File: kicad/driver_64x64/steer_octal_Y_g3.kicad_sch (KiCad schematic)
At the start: 66 parts

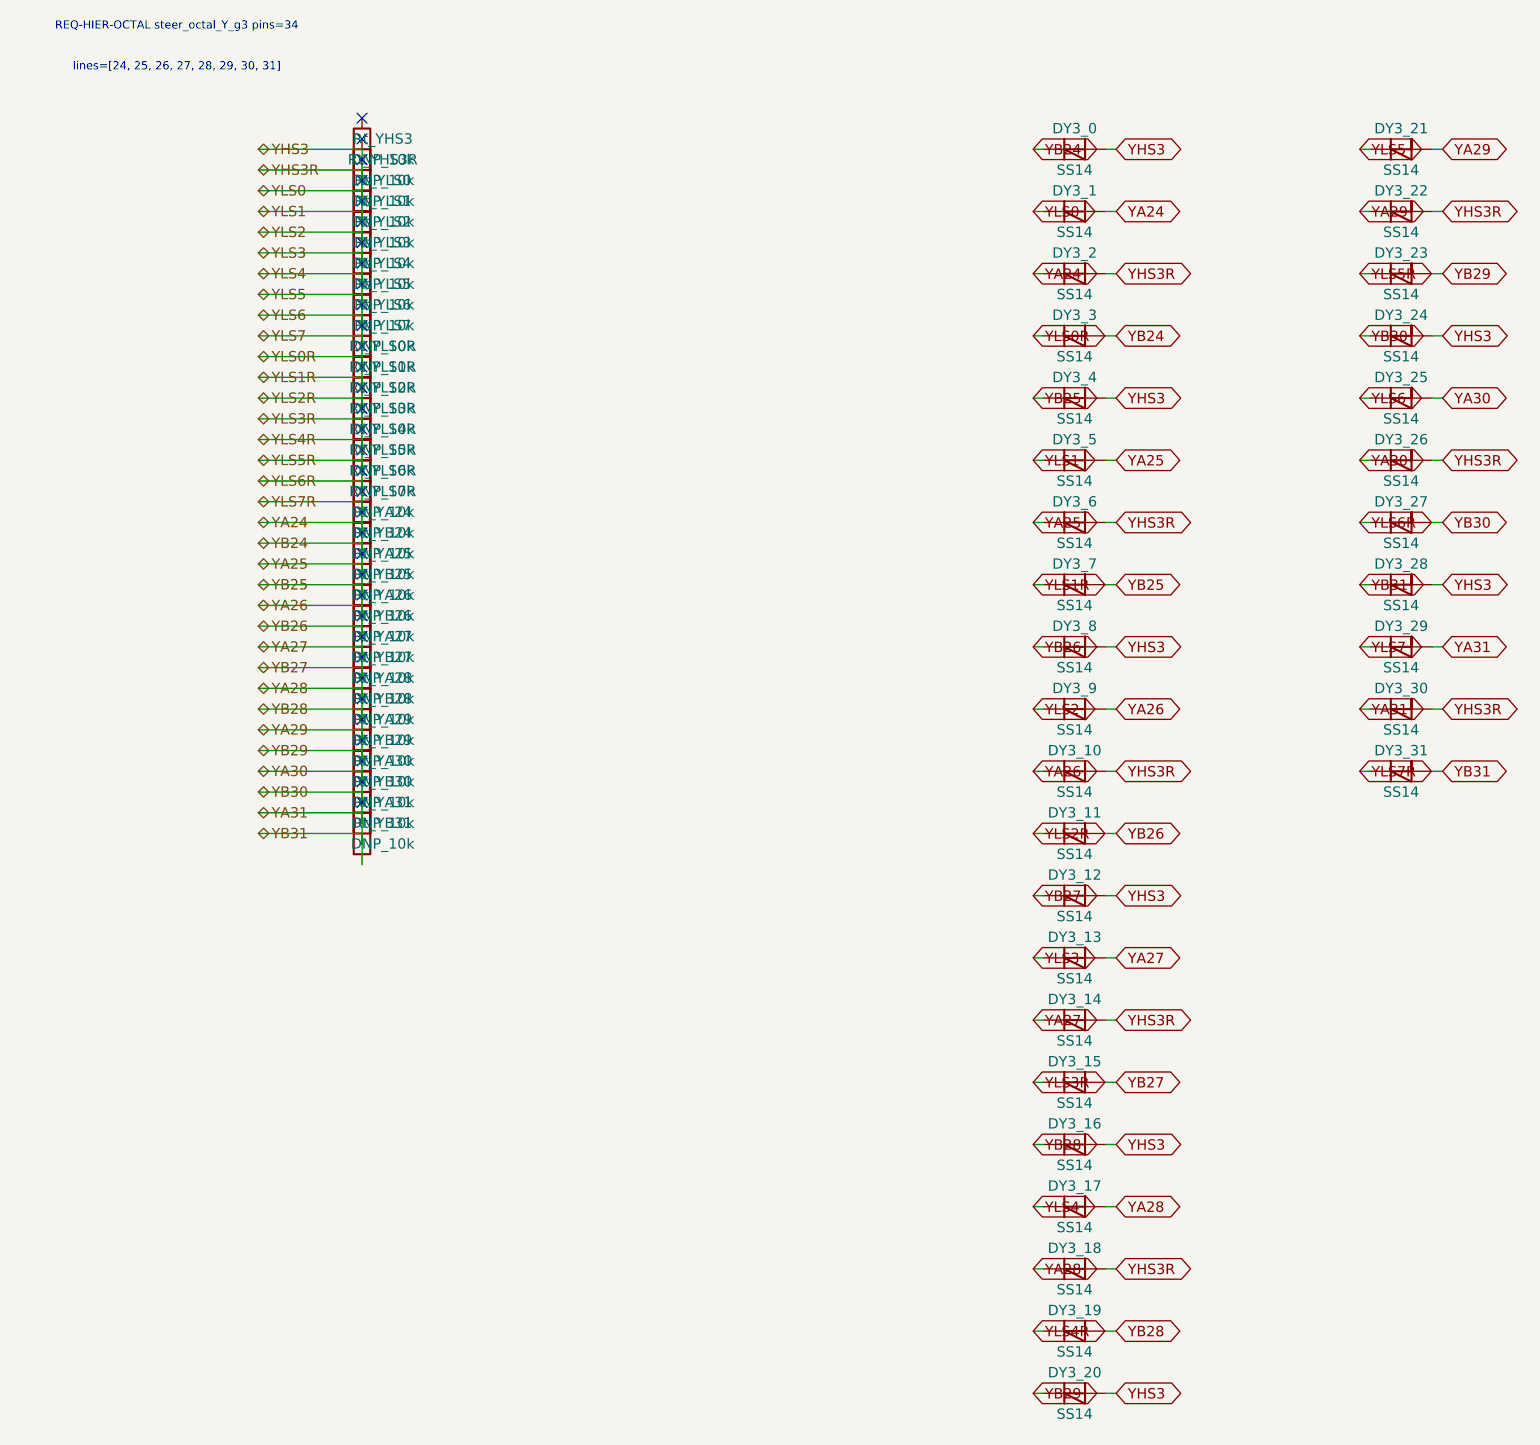
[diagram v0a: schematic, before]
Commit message: logical seperation into host and multiple decode/drive/steering boards
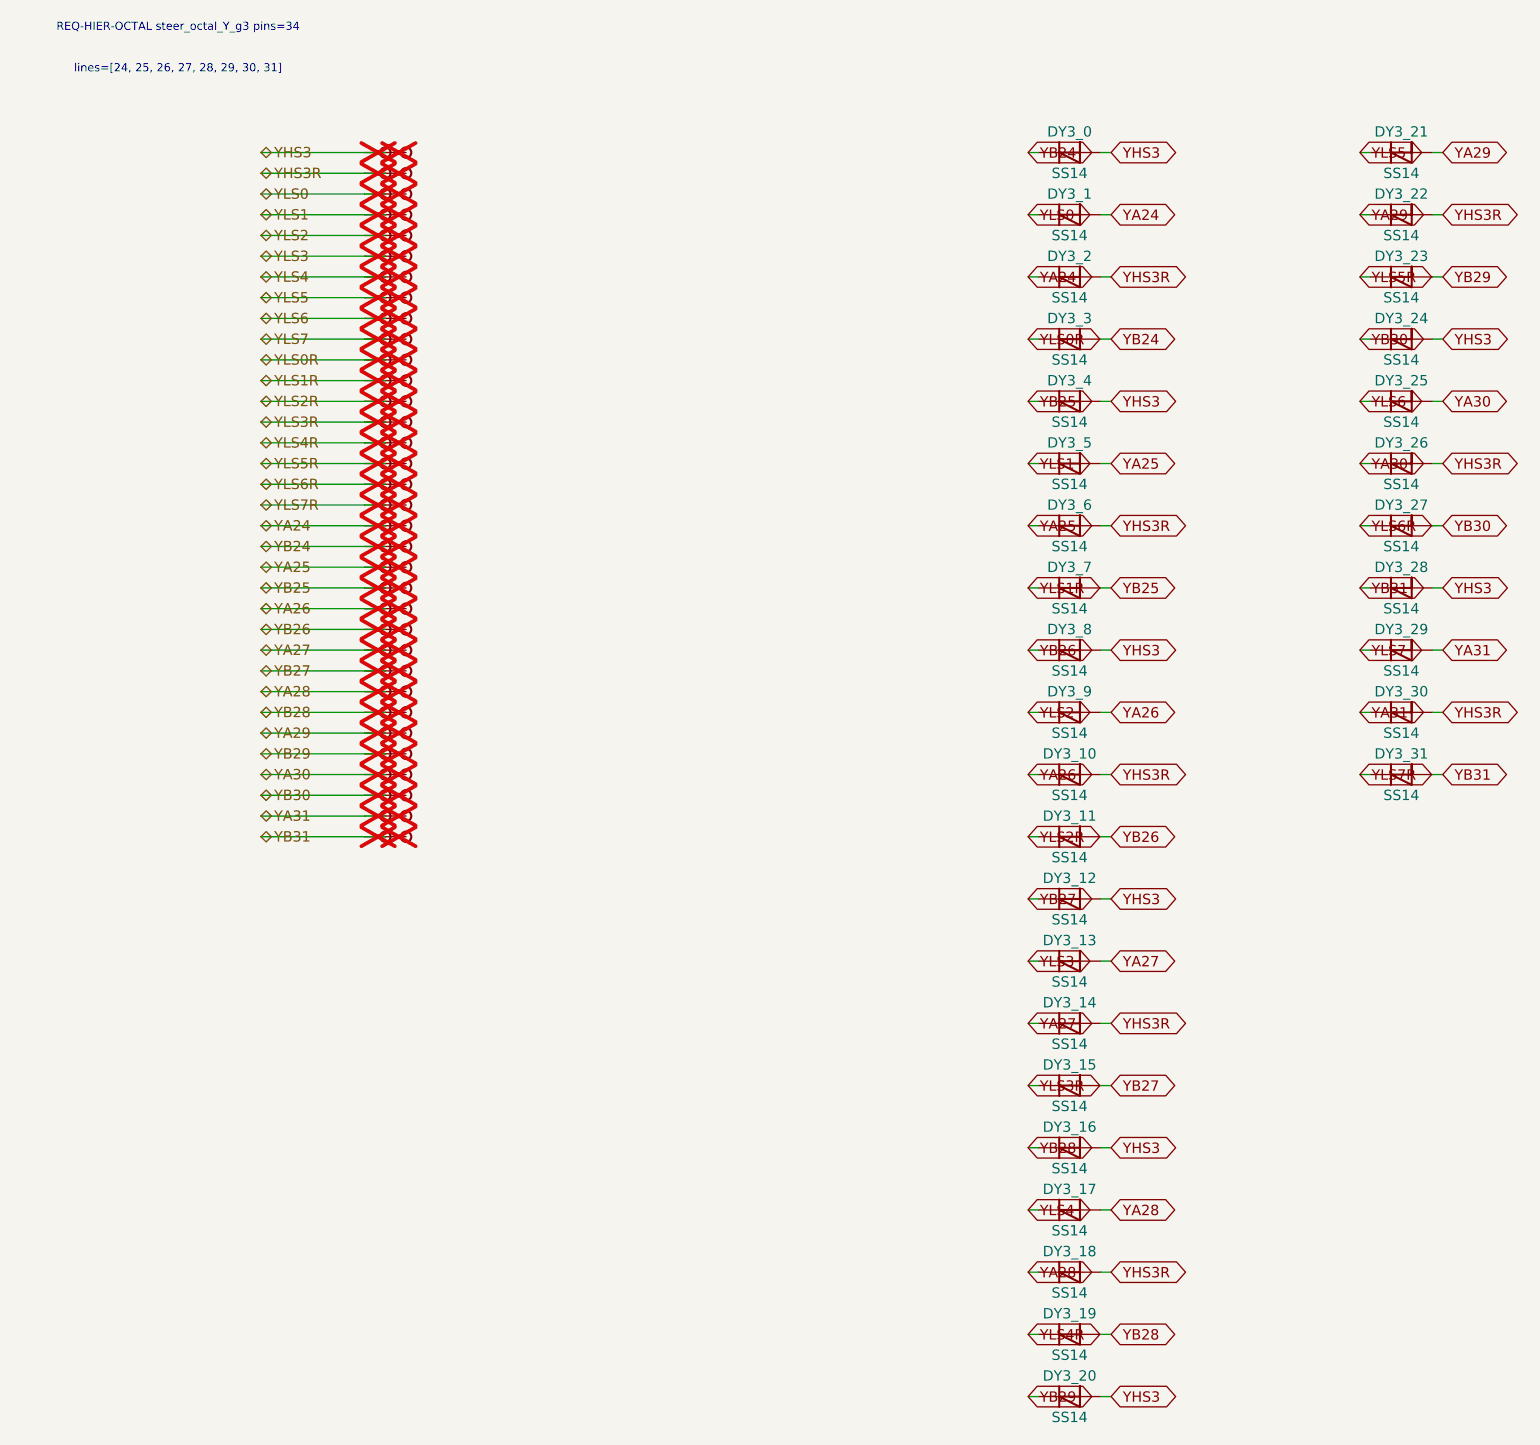
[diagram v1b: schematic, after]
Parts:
- removed Rt_YA24, Rt_YA25, Rt_YA26, Rt_YA27, Rt_YA28, Rt_YA29, Rt_YA30, Rt_YA31, Rt_YB24, Rt_YB25, Rt_YB26, Rt_YB27, Rt_YB28, Rt_YB29, Rt_YB30, Rt_YB31, Rt_YHS3, Rt_YHS3R, Rt_YLS0, Rt_YLS0R, Rt_YLS1, Rt_YLS1R, Rt_YLS2, Rt_YLS2R, Rt_YLS3, Rt_YLS3R, Rt_YLS4, Rt_YLS4R, Rt_YLS5, Rt_YLS5R, Rt_YLS6, Rt_YLS6R, Rt_YLS7, Rt_YLS7R: DNP_10k, symbol Device:R
- added TP_YA24, TP_YA24b, TP_YA25, TP_YA25b, TP_YA26, TP_YA26b, TP_YA27, TP_YA27b, TP_YA28, TP_YA28b, TP_YA29, TP_YA29b, TP_YA30, TP_YA30b, TP_YA31, TP_YA31b, TP_YB24, TP_YB24b, TP_YB25, TP_YB25b, TP_YB26, TP_YB26b, TP_YB27, TP_YB27b, TP_YB28, TP_YB28b, TP_YB29, TP_YB29b, TP_YB30, TP_YB30b, TP_YB31, TP_YB31b, TP_YHS3, TP_YHS3R, TP_YHS3Rb, TP_YHS3b, TP_YLS0, TP_YLS0R, TP_YLS0Rb, TP_YLS0b, TP_YLS1, TP_YLS1R, TP_YLS1Rb, TP_YLS1b, TP_YLS2, TP_YLS2R, TP_YLS2Rb, TP_YLS2b, TP_YLS3, TP_YLS3R, TP_YLS3Rb, TP_YLS3b, TP_YLS4, TP_YLS4R, TP_YLS4Rb, TP_YLS4b, TP_YLS5, TP_YLS5R, TP_YLS5Rb, TP_YLS5b, TP_YLS6, TP_YLS6R, TP_YLS6Rb, TP_YLS6b, TP_YLS7, TP_YLS7R, TP_YLS7Rb, TP_YLS7b: Stub, symbol CMR:Stub
- DY3_0, DY3_1, DY3_10, DY3_11, DY3_12, DY3_13, DY3_14, DY3_15, DY3_16, DY3_17, DY3_18, DY3_19, DY3_2, DY3_20, DY3_21, DY3_22, DY3_23, DY3_24, DY3_25, DY3_26, DY3_27, DY3_28, DY3_29, DY3_3, DY3_30, DY3_31, DY3_4, DY3_5, DY3_6, DY3_7, DY3_8, DY3_9: symbol Device:D_Schottky -> CMR:D_Schottky
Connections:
- net YA24: now also TP_YA24.1, TP_YA24b.1; no longer DY3_0.1 (K), DY3_0.2 (A), DY3_1.1 (K), DY3_10.1 (K), DY3_10.2 (A), DY3_11.1 (K), DY3_11.2 (A), DY3_12.1 (K), DY3_12.2 (A), DY3_13.1 (K), DY3_13.2 (A), DY3_14.1 (K), DY3_14.2 (A), DY3_15.1 (K), DY3_15.2 (A), DY3_16.1 (K), DY3_16.2 (A), DY3_17.1 (K), DY3_17.2 (A), DY3_18.1 (K), DY3_18.2 (A), DY3_19.1 (K), DY3_19.2 (A), DY3_2.2 (A), DY3_20.1 (K), DY3_20.2 (A), DY3_21.1 (K), DY3_21.2 (A), DY3_22.1 (K), DY3_22.2 (A), DY3_23.1 (K), DY3_23.2 (A), DY3_24.1 (K), DY3_24.2 (A), DY3_25.1 (K), DY3_25.2 (A), DY3_26.1 (K), DY3_26.2 (A), DY3_27.1 (K), DY3_27.2 (A), DY3_28.1 (K), DY3_28.2 (A), DY3_29.1 (K), DY3_29.2 (A), DY3_3.1 (K), DY3_3.2 (A), DY3_30.1 (K), DY3_30.2 (A), DY3_31.1 (K), DY3_31.2 (A), DY3_4.1 (K), DY3_4.2 (A), DY3_5.1 (K), DY3_5.2 (A), DY3_6.1 (K), DY3_6.2 (A), DY3_7.1 (K), DY3_7.2 (A), DY3_8.1 (K), DY3_8.2 (A), DY3_9.1 (K), DY3_9.2 (A)
- new net YA25: DY3_5.2 (A), DY3_6.1 (K), TP_YA25.1, TP_YA25b.1
- new net YA26: DY3_10.1 (K), DY3_9.2 (A), TP_YA26.1, TP_YA26b.1
- new net YA27: DY3_13.2 (A), DY3_14.1 (K), TP_YA27.1, TP_YA27b.1
- new net YA28: DY3_17.2 (A), DY3_18.1 (K), TP_YA28.1, TP_YA28b.1
- new net YA29: DY3_21.2 (A), DY3_22.1 (K), TP_YA29.1, TP_YA29b.1
- new net YA30: DY3_25.2 (A), DY3_26.1 (K), TP_YA30.1, TP_YA30b.1
- new net YA31: DY3_29.2 (A), DY3_30.1 (K), TP_YA31.1, TP_YA31b.1
- new net YB24: DY3_0.1 (K), DY3_3.2 (A), TP_YB24.1, TP_YB24b.1
- new net YB25: DY3_4.1 (K), DY3_7.2 (A), TP_YB25.1, TP_YB25b.1
- new net YB26: DY3_11.2 (A), DY3_8.1 (K), TP_YB26.1, TP_YB26b.1
- new net YB27: DY3_12.1 (K), DY3_15.2 (A), TP_YB27.1, TP_YB27b.1
- new net YB28: DY3_16.1 (K), DY3_19.2 (A), TP_YB28.1, TP_YB28b.1
- new net YB29: DY3_20.1 (K), DY3_23.2 (A), TP_YB29.1, TP_YB29b.1
- new net YB30: DY3_24.1 (K), DY3_27.2 (A), TP_YB30.1, TP_YB30b.1
- new net YB31: DY3_28.1 (K), DY3_31.2 (A), TP_YB31.1, TP_YB31b.1
- new net YHS3: DY3_0.2 (A), DY3_12.2 (A), DY3_16.2 (A), DY3_20.2 (A), DY3_24.2 (A), DY3_28.2 (A), DY3_4.2 (A), DY3_8.2 (A), TP_YHS3.1, TP_YHS3b.1
- new net YHS3R: DY3_10.2 (A), DY3_14.2 (A), DY3_18.2 (A), DY3_2.2 (A), DY3_22.2 (A), DY3_26.2 (A), DY3_30.2 (A), DY3_6.2 (A), TP_YHS3R.1, TP_YHS3Rb.1
- new net YLS0: DY3_1.1 (K), TP_YLS0.1, TP_YLS0b.1
- new net YLS0R: DY3_3.1 (K), TP_YLS0R.1, TP_YLS0Rb.1
- new net YLS1: DY3_5.1 (K), TP_YLS1.1, TP_YLS1b.1
- new net YLS1R: DY3_7.1 (K), TP_YLS1R.1, TP_YLS1Rb.1
- new net YLS2: DY3_9.1 (K), TP_YLS2.1, TP_YLS2b.1
- new net YLS2R: DY3_11.1 (K), TP_YLS2R.1, TP_YLS2Rb.1
- new net YLS3: DY3_13.1 (K), TP_YLS3.1, TP_YLS3b.1
- new net YLS3R: DY3_15.1 (K), TP_YLS3R.1, TP_YLS3Rb.1
- new net YLS4: DY3_17.1 (K), TP_YLS4.1, TP_YLS4b.1
- new net YLS4R: DY3_19.1 (K), TP_YLS4R.1, TP_YLS4Rb.1
- new net YLS5: DY3_21.1 (K), TP_YLS5.1, TP_YLS5b.1
- new net YLS5R: DY3_23.1 (K), TP_YLS5R.1, TP_YLS5Rb.1
- new net YLS6: DY3_25.1 (K), TP_YLS6.1, TP_YLS6b.1
- new net YLS6R: DY3_27.1 (K), TP_YLS6R.1, TP_YLS6Rb.1
- new net YLS7: DY3_29.1 (K), TP_YLS7.1, TP_YLS7b.1
- new net YLS7R: DY3_31.1 (K), TP_YLS7R.1, TP_YLS7Rb.1
- no-connect marks 34 -> 0
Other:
- moved on the sheet: DY3_0, DY3_1, DY3_10, DY3_11, DY3_12, DY3_13, DY3_14, DY3_15, DY3_16, DY3_17, DY3_18, DY3_19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
